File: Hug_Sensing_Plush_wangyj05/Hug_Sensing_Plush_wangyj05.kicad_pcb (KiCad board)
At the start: 2 copper layers, 100 x 100 mm, 62 parts, among them J1 USB_C_Receptacle_USB2.0_16P, J2 Header B2B-PH-SM4-TBLFSN, SW1 SW_SPST, SW2 SW_SPST, U1 BQ24040DSQR, U2 TPS63802DLAR, U3 ESP32-S3-WROOM-1-N4, U4 DRV2605LDGS, U5 USBLC6-2SC6, U6 MPRLS0025PA00001A

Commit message: Hug-Sensing IoT Plush
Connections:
- C10 pad 2: Net-(U5-VBUS) -> +5V
- U5 pad 5: Net-(U5-VBUS) -> +5V

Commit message: Edited board layout
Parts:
- added J3: Wire Pad, Connector_Wire:SolderWirePad_1x01_SMD_1x2mm, F.Cu at (93.9, 55.1)
- added J4: Wire Pad, Connector_Wire:SolderWirePad_1x01_SMD_1x2mm, F.Cu at (96.3, 55.1)
- added J5: Wire Pad, Connector_Wire:SolderWirePad_1x01_SMD_1x2mm, F.Cu at (100.9, 53.1)
- added J6: Wire Pad, Connector_Wire:SolderWirePad_1x01_SMD_1x2mm, F.Cu at (103.3, 53.1)
- moved R16 65.8 mm to (107.4, 72.4), turned to 180 degrees
- moved TP6 64.3 mm to (60.5, 44.4)
- moved SW1 60.8 mm to (56.0, 48.9), turned to -90 degrees
- moved H2 59.7 mm to (107.0, 76.0), turned to 180 degrees
- moved R14 58.3 mm to (60.3, 52.6)
- moved C11 58.3 mm to (60.3, 50.1)
- moved C9 58.3 mm to (60.3, 47.6)
- moved R15 56.6 mm to (55.2, 72.6), turned to 180 degrees
- moved SW2 55.3 mm to (64.7, 49.0), turned to 90 degrees
- moved H1 49.4 mm to (56.0, 76.0), turned to 180 degrees
- moved R8 46.5 mm to (89.9, 65.0)
- moved TP10 46.5 mm to (85.1, 71.8)
- moved TP8 46.5 mm to (85.1, 64.3)
- moved TP9 46.5 mm to (85.1, 68.1)
- moved C5 46.5 mm to (89.9, 60.0)
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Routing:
- net +5V: track 0.00 -> 41.4 mm
- net Net-(D1-A): track 0.00 -> 22.4 mm
- net Net-(D1-K): track 0.00 -> 18.2 mm, vias 0 -> 1
- net Net-(D2-A): track 0.00 -> 18.1 mm
- net /USB-C Connector/D+: track 0.00 -> 16.4 mm
- net Net-(U1-PRETERM): track 0.00 -> 14.4 mm, vias 0 -> 1
- net /USB-C Connector/D-: track 0.00 -> 11.6 mm
- net Net-(U1-ISET): track 0.00 -> 11.6 mm, vias 0 -> 1
- net Net-(J1-CC2): track 0.00 -> 10.6 mm
- net Net-(D2-K): track 0.00 -> 10.5 mm, vias 0 -> 1
- net /Battery and Battery Charger/TS: track 0.00 -> 9.97 mm
- net Net-(J1-CC1): track 0.00 -> 7.83 mm
- net Net-(H3-Pad1): track 0.00 -> 6.42 mm
- net Battery_3V_4V2: track 0.00 -> 5.47 mm
- net Net-(H4-Pad1): track 0.00 -> 4.74 mm
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- added copper zone on F.Cu, net Battery_3V_4V2
- added copper zone on F.Cu, net GND
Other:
- board size 100 x 100 mm -> 58.9 x 45 mm
- board text removed: "Battery charger"
- board text removed: "Buck-boost converter"
- board text removed: "ESP32"
- board text removed: "Motor Driver"
- board text removed: "Pressure sensor"
- board text removed: "USB-C"

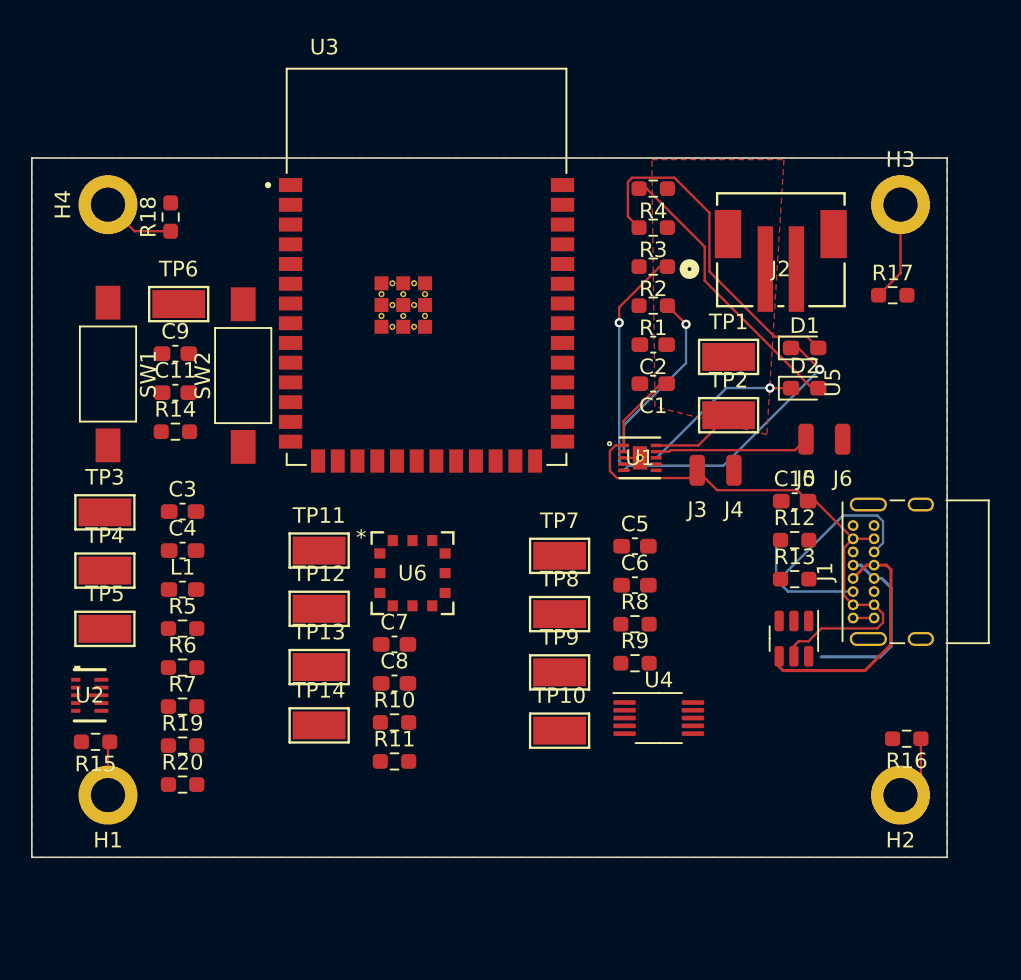
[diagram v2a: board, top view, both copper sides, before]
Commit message: Updated layout
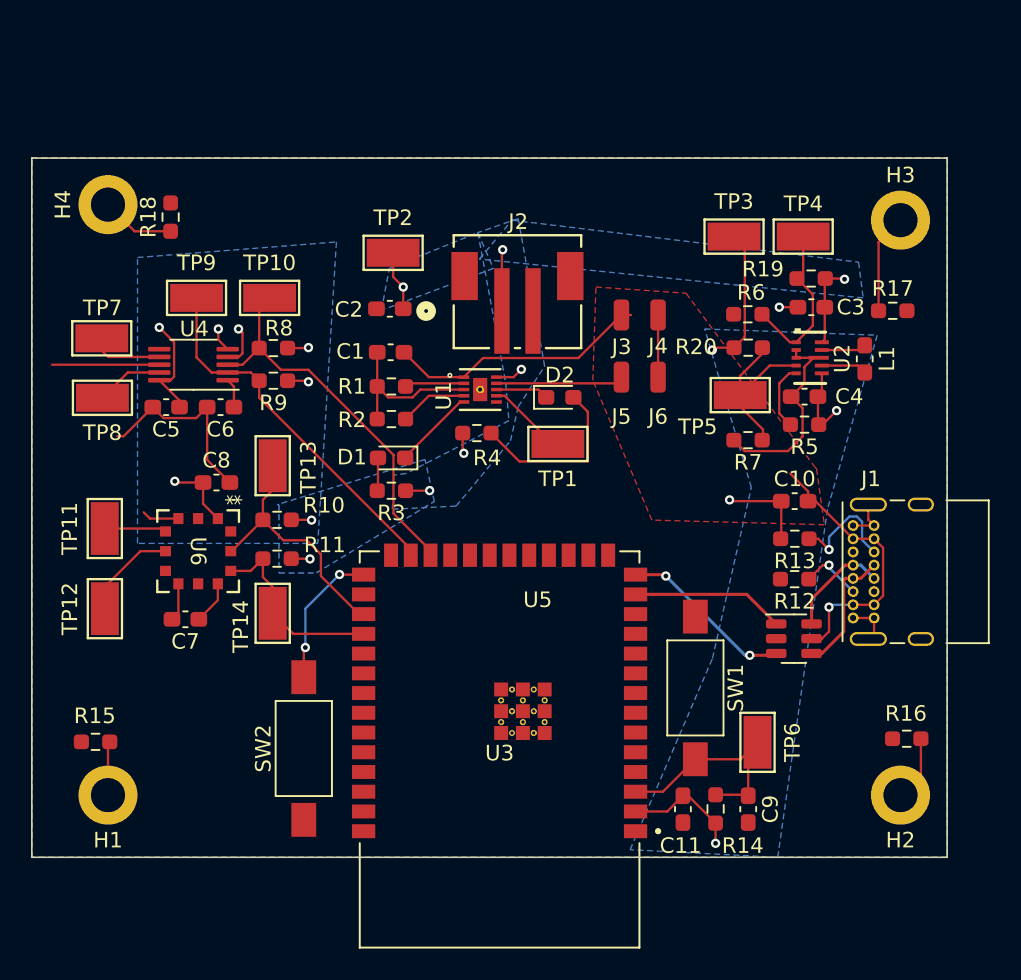
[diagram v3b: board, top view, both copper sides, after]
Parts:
- moved U2 51.2 mm to (101.2, 47.9)
- moved R19 50.4 mm to (101.3, 42.8), turned to 180 degrees
- moved TP4 49.8 mm to (100.7, 40.1)
- moved R20 47.3 mm to (97.2, 45.1), turned to 180 degrees
- moved C9 47.1 mm to (97.2, 76.9), turned to -90 degrees
- moved TP6 46.7 mm to (97.8, 72.6), turned to -90 degrees
- moved L1 46.3 mm to (104.7, 47.9), turned to -90 degrees
- moved TP3 44.2 mm to (96.3, 40.1)
- moved TP5 43.6 mm to (96.7, 50.3)
- moved SW1 42.9 mm to (93.8, 69.1)
- moved C3 42.5 mm to (101.3, 44.6), turned to 180 degrees
- moved R14 42.4 mm to (95.1, 76.9), turned to 90 degrees
- moved C11 42.3 mm to (93.0, 76.9), turned to -90 degrees
- moved R5 42.1 mm to (100.8, 52.2), turned to 180 degrees
- moved R6 41.8 mm to (97.2, 47.2)
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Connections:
- U1 pad V: (no net) -> GND
- U3 pad 24: unconnected-(U3-IO47-Pad24) -> /motor_sda
- U3 pad 25: unconnected-(U3-IO48-Pad25) -> /motor_scl
- U3 pad 29: /motor_scl -> /ESP32/SDA_sensor
- U3 pad 30: /motor_sda -> /ESP32/SCL_sensor
- U3 pad 4: /ESP32/SDA_sensor -> unconnected-(U3-IO4-Pad4)
- U3 pad 41_10: (no net) -> GND
- U3 pad 41_11: (no net) -> GND
- U3 pad 41_12: (no net) -> GND
- U3 pad 41_13: (no net) -> GND
- U3 pad 41_14: (no net) -> GND
- U3 pad 41_15: (no net) -> GND
- U3 pad 41_16: (no net) -> GND
- U3 pad 41_17: (no net) -> GND
- U3 pad 41_18: (no net) -> GND
- U3 pad 41_19: (no net) -> GND
- U3 pad 41_20: (no net) -> GND
- U3 pad 41_21: (no net) -> GND
- U3 pad 5: /ESP32/SCL_sensor -> unconnected-(U3-IO5-Pad5)
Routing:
- net GND: track 1.90 -> 65.2 mm, vias 0 -> 3
- net Battery_3V_4V2: track 5.47 -> 36.3 mm, vias 0 -> 13
- net /motor_sda: track 0.00 -> 25.1 mm
- net /motor_scl: track 0.00 -> 23.8 mm
- net +3.3V: track 0.00 -> 21.7 mm, vias 0 -> 3
- net Net-(D1-A): track 22.4 -> 2.13 mm
- net /ESP32/SDA_sensor: track 0.00 -> 16.0 mm
- net Net-(SW1-B): track 0.00 -> 15.0 mm
- net Net-(D1-K): track 18.2 -> 5.37 mm, vias 1 -> 0
- net /ESP32/SCL_sensor: track 0.00 -> 12.0 mm
- net Net-(U2-FB): track 0.00 -> 11.4 mm
- net /ESP32/ESP32_USB_D+: track 0.00 -> 11.3 mm, vias 0 -> 2
- net Net-(U2-EN): track 0.00 -> 10.8 mm
- net Net-(U1-PRETERM): track 14.4 -> 4.37 mm, vias 1 -> 0
- net /ESP32/ESP32_USB_D-: track 0.00 -> 9.84 mm
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- added copper zone on B.Cu, net +3.3V
- added copper zone on F.Cu, net +5V
- added copper zone on B.Cu, net Battery_3V_4V2
- added copper zone on B.Cu, net GND
- removed copper zone on F.Cu, net Battery_3V_4V2
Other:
- board text added: "Charger"
- board text added: "Converter"
- board text added: "ESP"
- board text added: "ESP32"
- board text added: "Motor Driver"
- board text added: "Sensor"
- board text added: "USB"

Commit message: Edited PCB layout
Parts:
- C10, J1, R12, R13, U5: moved to B.Cu
- moved R3 22.1 mm to (90.7, 41.6), turned to 0 degrees
- moved D1 19.4 mm to (90.7, 44.0), turned to 0 degrees
- moved TP2 17.3 mm to (84.8, 54.9), turned to 180 degrees
- moved R2 17.3 mm to (90.7, 46.6), turned to 0 degrees
- moved C1 17.0 mm to (90.8, 51.2), turned to 0 degrees
- moved R1 16.5 mm to (90.7, 49.0), turned to 0 degrees
- moved J6 13.2 mm to (78.7, 52.7), turned to 0 degrees
- moved C2 12.7 mm to (85.0, 51.3), turned to 0 degrees
- moved J3 9.89 mm to (91.8, 54.6), turned to 0 degrees
- moved J4 9.70 mm to (89.4, 54.6), turned to 0 degrees
- moved J5 8.72 mm to (81.1, 52.7), turned to 0 degrees
- moved TP1 8.42 mm to (80.4, 46.3), turned to 180 degrees
- moved SW1 7.32 mm to (99.8, 73.4), turned to 90 degrees
- moved R13 5.92 mm to (100.7, 65.4)
- moved R14 5.91 mm to (93.7, 71.2), turned to 180 degrees
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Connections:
- J2 pad 3: (no net) -> GND
- J2 pad 4: (no net) -> GND
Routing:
- net Battery_3V_4V2: track 36.3 -> 115.7 mm, vias 13 -> 8
- net GND: track 65.2 -> 47.7 mm, vias 3 -> 44
- net +3.3V: track 21.7 -> 9.65 mm, vias 3 -> 0
- net Net-(D2-A): track 11.5 -> 2.23 mm
- net Net-(SW1-B): track 15.0 -> 20.4 mm, vias 0 -> 2
- net /USB-C Connector/D+: track 8.32 -> 4.78 mm
- net +5V: track 35.3 -> 38.6 mm
- net /USB-C Connector/D-: track 6.88 -> 4.60 mm
- net /Battery and Battery Charger/TS: track 8.21 -> 5.95 mm
- net Net-(H3-Pad1): track 6.42 -> 4.84 mm
- net /ESP32/ESP32_USB_D+: track 11.3 -> 10.1 mm, vias 2 -> 1
- net /motor_sda: track 25.1 -> 24.0 mm
- net Net-(J1-CC1): track 4.01 -> 3.09 mm, vias 1 -> 0
- net /ESP32/ESP32_USB_D-: track 9.84 -> 9.70 mm, vias 0 -> 1
- added copper zone on F.Cu, net +3.3V
- removed copper zone on B.Cu, net +3.3V
- removed copper zone on F.Cu, net +5V
- removed copper zone on B.Cu, net Battery_3V_4V2

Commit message: Updated board layout
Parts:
- added H5: EECS Logo, Project Library:EECSLogo, B.Cu at (73.7, 36.8)
- added H6: MechELogo, Project Library:MechELogo, B.Cu at (69.5, 71.7)
- added H7: EdgertonLogo, Project Library:EdgertonLogo, B.Cu at (85.6, 61.4)
- added TP15: TestPoint, TestPoint:TestPoint_Keystone_5015_Micro-Minature, F.Cu at (90.7, 43.6)
- added TP16: TestPoint, TestPoint:TestPoint_Keystone_5015_Micro-Minature, F.Cu at (90.2, 51.2)
- added kibuzzard-65AAE9C3: G***, kibuzzard-65AAE9C3, F.Cu at (65.6, 36.2)
- added kibuzzard-65AAE9E5: G***, kibuzzard-65AAE9E5, F.Cu at (90.4, 36.3)
- added kibuzzard-65AAEA37: G***, kibuzzard-65AAEA37, F.Cu at (98.7, 36.2)
- added kibuzzard-65AAEA43: G***, kibuzzard-65AAEA43, F.Cu at (107.7, 56.0)
- added kibuzzard-65AAEA4C: G***, kibuzzard-65AAEA4C, F.Cu at (73.4, 58.5)
- added kibuzzard-65AAEA55: G***, kibuzzard-65AAEA55, F.Cu at (53.2, 53.9)
- added kibuzzard-65AAEA96: G***, kibuzzard-65AAEA96, F.Cu at (52.6, 50.5)
- added kibuzzard-65AAEAAB: G***, kibuzzard-65AAEAAB, F.Cu at (62.4, 42.1)
- added kibuzzard-65AAEAD5: G***, kibuzzard-65AAEAD5, F.Cu at (52.6, 46.2)
- added kibuzzard-65AAEADF: G***, kibuzzard-65AAEADF, F.Cu at (68.2, 42.1)
- added kibuzzard-65AAEB64: G***, kibuzzard-65AAEB64, F.Cu at (83.9, 45.4)
- added kibuzzard-65AAEBD9: G***, kibuzzard-65AAEBD9, F.Cu at (75.6, 50.5)
- added kibuzzard-65AAEBEE: G***, kibuzzard-65AAEBEE, F.Cu at (94.9, 42.1)
- added kibuzzard-65AAECF1: G***, kibuzzard-65AAECF1, F.Cu at (100.8, 38.1)
- added kibuzzard-65AAF1CD: G***, kibuzzard-65AAF1CD, F.Cu at (92.9, 40.9)
- added kibuzzard-65AAF1FE: G***, kibuzzard-65AAF1FE, F.Cu at (91.4, 53.0)
- added kibuzzard-65AAF250: G***, kibuzzard-65AAF250, F.Cu at (96.0, 52.0)
- added kibuzzard-65AAF270: G***, kibuzzard-65AAF270, F.Cu at (92.3, 55.0)
- added kibuzzard-65AAF2C1: G***, kibuzzard-65AAF2C1, F.Cu at (75.7, 42.5)
- added kibuzzard-65AAF2E5: G***, kibuzzard-65AAF2E5, F.Cu at (66.1, 74.8)
- added kibuzzard-65AAF304: G***, kibuzzard-65AAF304, F.Cu at (95.6, 77.9)
- added kibuzzard-65AAF374: G***, kibuzzard-65AAF374, F.Cu at (95.1, 65.1)
- added kibuzzard-65AAF38A: G***, kibuzzard-65AAF38A, F.Cu at (55.9, 56.1)
- added kibuzzard-65AAF394: G***, kibuzzard-65AAF394, F.Cu at (55.8, 66.6)
- added kibuzzard-65AAF39C: G***, kibuzzard-65AAF39C, F.Cu at (64.8, 53.9)
- added kibuzzard-65AAF3AD: G***, kibuzzard-65AAF3AD, F.Cu at (65.3, 67.9)
- added kibuzzard-65AAF7C7: G***, kibuzzard-65AAF7C7, B.Cu at (82.3, 76.2)
- C10, R12, R13, U5: moved to F.Cu
- J3: value Wire Pad -> Charger Header 5V
- J4: value Wire Pad -> Charger Header GND
- J5: value Wire Pad -> Thermistor Header TS
- J6: value Wire Pad -> Thermistor Header GND
- TP6: value TestPoint -> TP: ESP_EN
- moved TP2 9.58 mm to (75.5, 52.4)
- moved C1 4.79 mm to (86.0, 51.9), turned to -90 degrees
- moved R3 2.65 mm to (90.7, 39.0)
- moved D1 2.58 mm to (90.7, 41.5)
- moved C10 2.28 mm to (100.6, 59.6)
- moved R12 2.22 mm to (100.7, 57.3)
- moved SW1 1.62 mm to (98.2, 73.7)
- moved TP6 1.57 mm to (93.9, 67.1)
- moved R14 1.03 mm to (93.5, 70.2)
- moved C2 1.01 mm to (84.1, 51.9), turned to -90 degrees
- moved J3 0.97 mm to (91.1, 55.2)
- moved J4 0.97 mm to (88.7, 55.2)
- moved C11 0.43 mm to (93.4, 75.1)
- moved C9 0.40 mm to (93.5, 72.6)
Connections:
- U5 pad 1: /ESP32/ESP32_USB_D- -> /ESP32/ESP32_USB_D+
- U5 pad 3: /ESP32/ESP32_USB_D+ -> /ESP32/ESP32_USB_D-
- U5 pad 4: /USB-C Connector/D+ -> /USB-C Connector/D-
- U5 pad 6: /USB-C Connector/D- -> /USB-C Connector/D+
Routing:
- net +3.3V: track 9.65 -> 19.8 mm, vias 0 -> 4
- net Net-(SW1-B): track 20.4 -> 15.6 mm, vias 2 -> 0
- net GND: track 47.7 -> 43.9 mm, vias 44 -> 43
- net Battery_3V_4V2: track 115.7 -> 119.3 mm
- net Net-(U1-PRETERM): track 4.66 -> 7.89 mm
- net +5V: track 38.6 -> 35.4 mm
- net Net-(D1-K): track 5.78 -> 8.30 mm
- net Net-(U1-ISET): track 3.83 -> 6.21 mm
- net Net-(J1-CC2): track 7.49 -> 5.64 mm, vias 1 -> 0
- net Net-(J1-CC1): track 3.09 -> 4.91 mm
- net /ESP32/ESP32_USB_D+: vias 1 -> 0
- net /ESP32/ESP32_USB_D-: track 9.70 -> 9.68 mm, vias 1 -> 0
- added copper zone on B.Cu, net +3.3V
- removed copper zone on F.Cu, net +3.3V
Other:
- board size 58.9 x 45 mm -> 60 x 45 mm
- board text removed: "Charger"
- board text removed: "Converter"
- board text removed: "ESP"
- board text removed: "ESP32"
- board text removed: "Motor Driver"
- board text removed: "Sensor"
- board text removed: "USB"
